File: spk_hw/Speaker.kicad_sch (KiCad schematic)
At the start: 16 parts, among them SW1 SW_SPST, U1 CH591F, U2 MAX98357A, U4 ME6206A33XG, Y1 32MHz

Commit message: spk_hw: Add DC-DC (Migration@tangibles)
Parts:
- added L1: 22u, Inductor_SMD:L_Sunlord_SWPA252012S, symbol Device:L
- C1: value 100n -> 2.2u
- C2: value 1u -> 2.2u
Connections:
- net VDCID: now also L1.1; no longer U1.4 (VSW)
- new net: L1.2, U1.4 (VSW)
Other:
- moved on the sheet: C2

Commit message: spk_hw: Finish schematic, finally >-<
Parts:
- removed SW1: SW_SPST, symbol Switch:SW_SPST
- added C2, C41, C7: 100n, Capacitor_SMD:C_0402_1005Metric, symbol Device:C
- added C31, C32, C33: 10u, Capacitor_SMD:C_0402_1005Metric, symbol Device:C
- added C61, C62, C63, C64: 10u, Capacitor_SMD:C_0603_1608Metric, symbol Device:C
- added C90: 1.5F 5.5V, Capacitor_THT:DX_5R5VxxxxU_D19.0mm_P5.00mm, symbol Device:C_Polarized
- added D2: 1N5819, Diode_SMD:D_SOD-323, symbol Device:D
- added J1: Conn_01x04, TestPoints_P2.00:TestPoints_1x04_P2.00, symbol Connector_Generic:Conn_01x04
- added L2: 2.2u, Inductor_SMD:L_Sunlord_SWPA252012S, symbol Device:L
- added L3: 22u, Inductor_SMD:L_Sunlord_SWPA252012S, symbol Device:L
- added R2, R31: 750k, Resistor_SMD:R_0402_1005Metric, symbol Device:R
- added R3: 100k, Resistor_SMD:R_0402_1005Metric, symbol Device:R
- added R32: 200k, Resistor_SMD:R_0402_1005Metric, symbol Device:R
- added R41, R42: 1M, Resistor_SMD:R_0402_1005Metric, symbol Device:R
- added SC1: Solar_Cell, Connector_JST:JST_PH_S2B-PH-SM4-TB_1x02-1MP_P2.00mm_Horizontal, symbol Device:Solar_Cell
- added SW1: SW_Push, Button_Switch_SMD:SW_SPST_SKQG_WithStem, symbol Switch:SW_Push
- added U3: TPS61099DRV, Package_SON:WSON-6-1EP_2x2mm_P0.65mm_EP1x1.6mm, symbol Regulator_Switching:TPS61099DRV
- added U4: XS3A1T3157, XS3A1T3157:XS3A1T3157GSH, symbol XS3A1T3157:XS3A1T3157
- added U6: MT3608L, Package_TO_SOT_SMD:SOT-23-6, symbol Regulator_Switching:MT3608
- C4: renamed from C3; value 1u -> 2.2u
- C6: renamed from C5; value 100n -> 10u; footprint Capacitor_SMD:C_0402_1005Metric -> Capacitor_SMD:C_0603_1608Metric
- L1: Mfr PN (none) -> SWPA252012S220MT
- LS1: footprint (none) -> Connector_JST:JST_PH_S2B-PH-SM4-TB_1x02-1MP_P2.00mm_Horizontal
- U5: renamed from U4; value ME6206A33XG -> XC6206P332; LCSC PN (none) -> C5446
- renumbered C2 to C3, C4 to C5, C7 to C51, C8 to C52
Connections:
- net BOOT_ACT: now also R1.1; no longer D1.1 (K)
- net GND: now also D1.1 (K), LS1.MP, C2.2, C31.1, C32.1, C33.1, C41.1, C61.1, C62.1, C63.1, C64.1, C7.1, C90.2, J1.2 (Pin_2), R3.2, R32.2, R41.2, R42.1, SC1.2 (-), SC1.MP, U3.1 (GND), U3.7 (GND), U4.2 (GND), U6.2 (GND)
- net VBAT: now also C32.2, C33.2, C41.2, C90.1, R31.1, SW1.1, U3.2 (VOUT), U4.1 (Y2), U4.5 (VCC); no longer C51.2, U5.3 (VI)
- net PWR_LATCH: now reaches U1.10 (PB13/SCK0_/TXD1_/DCD_)
- net PWR_LATCH: now also R41.1, U4.6 (S)
- net RXD: now reaches U1.6 (PA8/RXD1)
- net RXD: now also J1.3 (Pin_3)
- net TXD: now reaches U1.7 (PA9/TMR0/TXD1)
- net TXD: now also J1.4 (Pin_4)
- net BTN: now reaches U1.9 (PB14/TIO/MOSI_/PWM10/DSR)
- net BTN: now also R42.2, SW1.2, U4.3 (Y1)
- net VDD renamed +3.3V
- net +3.3V: now also C2.1, J1.1 (Pin_1); no longer C6.2, R1.1, U2.A1 (~{SD_MODE}), U2.A2 (VDD)
- new net: C31.2, L2.1, SC1.1 (+), U3.4 (EN), U3.6 (VI)
- new net: R31.2, R32.1, U3.3 (FB)
- new net: L2.2, U3.5 (SW)
- new net: D2.2 (A), L3.2, U6.1 (SW)
- new net: R2.2, R3.1, U6.3 (FB)
- new net +5V: C6.2, C63.2, C64.2, C7.2, D2.1 (K), R2.1, U2.A1 (~{SD_MODE}), U2.A2 (VDD)
- new net VBAT_SW: C51.2, C61.2, C62.2, L3.1, U4.4 (Z), U5.3 (VI), U6.4 (EN), U6.5 (IN)
- no-connect marks 17 -> 13
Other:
- note added: "0.6 V typ."
- note added: "1.0 V typ."
- note added: "4.75 V"
- note added: "5.1 V"
- note added: "Shorting the LED pulls BOOT low; LED's Vf is large enough. To be absolutely sure, set BOOT to PB11 in user configuration"
- note added: "min. 50 nA * 100 = 5 uA max. 1 V / 5 uA = 200 kOhm"
- moved on the sheet: AE1, C1, C3, C4, C5, C51, C52, C6, D1, L1, R1, U1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

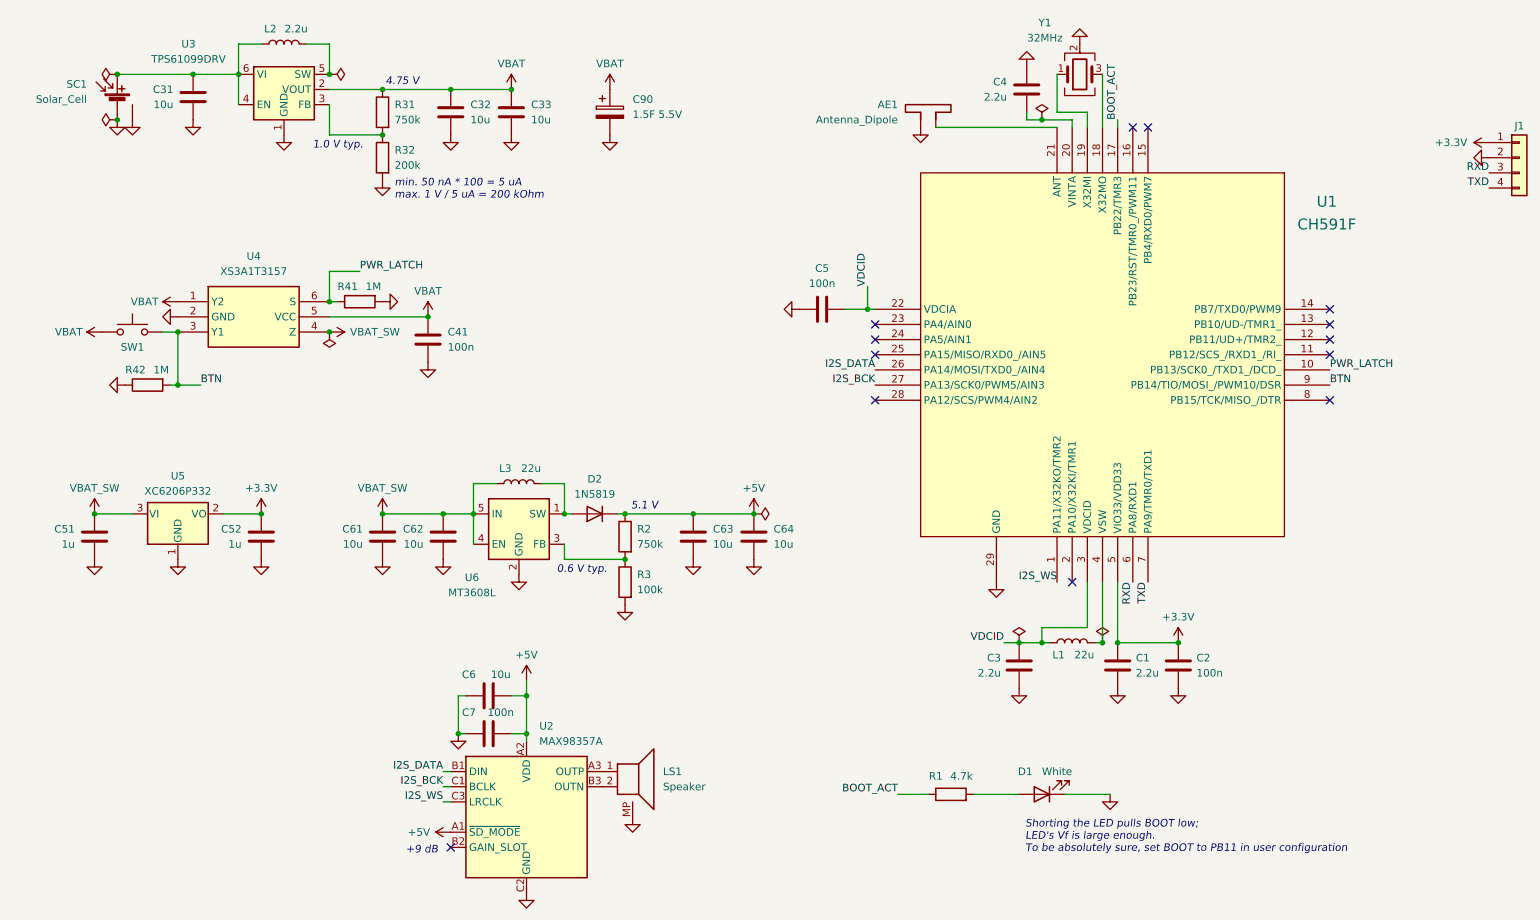
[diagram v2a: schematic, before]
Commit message: spk_hw: Board layout and routing
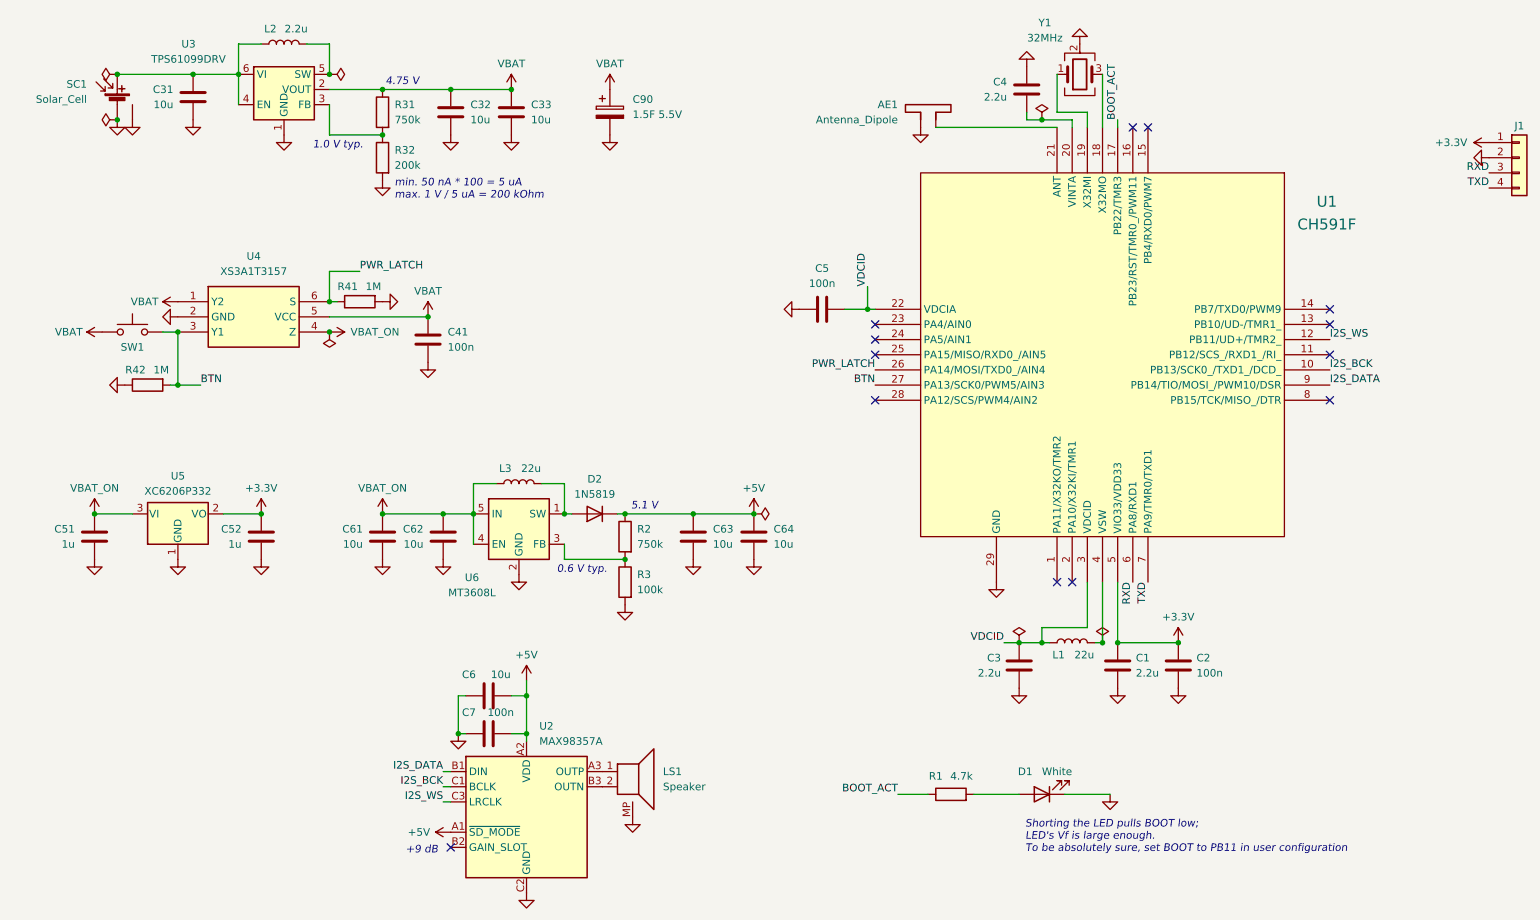
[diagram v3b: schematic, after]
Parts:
- C31, C32, C33: footprint Capacitor_SMD:C_0402_1005Metric -> Capacitor_SMD:C_0603_1608Metric
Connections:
- net BTN: now also U1.27 (PA13/SCK0/PWM5/AIN3); no longer U1.9 (PB14/TIO/MOSI_/PWM10/DSR)
- net I2S_BCK: now also U1.10 (PB13/SCK0_/TXD1_/DCD_); no longer U1.27 (PA13/SCK0/PWM5/AIN3)
- net I2S_DATA: now also U1.9 (PB14/TIO/MOSI_/PWM10/DSR); no longer U1.26 (PA14/MOSI/TXD0_/AIN4)
- net I2S_WS: now also U1.12 (PB11/UD+/TMR2_); no longer U1.1 (PA11/X32KO/TMR2)
- net PWR_LATCH: now also U1.26 (PA14/MOSI/TXD0_/AIN4); no longer U1.10 (PB13/SCK0_/TXD1_/DCD_)
- net VBAT_SW renamed VBAT_ON
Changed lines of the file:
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@@
 	)
 	(no_connect
+		(at 189.23 114.3)
+	)
+	(no_connect
 		(at 158.75 76.2)
 	)
@@
 	)
 	(no_connect
-		(at 234.95 73.66)
-	)
-	(no_connect
 		(at 234.95 68.58)
 	)
@@
 	)
 	(label "I2S_BCK"
-		(at 158.75 81.28 180)
+		(at 234.95 78.74 0)
 		(effects
 			(font
 				(size 1.27 1.27)
 			)
-			(justify right bottom)
+			(justify left bottom)
 		)
 	)
@@
 	)
 	(label "PWR_LATCH"
-		(at 234.95 78.74 0)
+		(at 158.75 78.74 180)
 		(effects
 			(font
 				(size 1.27 1.27)
 			)
-			(justify left bottom)
+			(justify right bottom)
 		)
 	)
@@
 	)
 	(label "I2S_WS"
-		(at 189.23 114.3 180)
+		(at 234.95 73.66 0)
 		(effects
 			(font
 				(size 1.27 1.27)
 			)
-			(justify right bottom)
+			(justify left bottom)
 		)
 	)
@@
 	)
 	(label "BTN"
-		(at 234.95 81.28 0)
+		(at 158.75 81.28 180)
 		(effects
 			(font
 				(size 1.27 1.27)
 			)
-			(justify left bottom)
+			(justify right bottom)
 		)
 	)
@@
 	)
 	(label "I2S_DATA"
-		(at 158.75 78.74 180)
+		(at 234.95 81.28 0)
 		(effects
 			(font
 				(size 1.27 1.27)
 			)
-			(justify right bottom)
+			(justify left bottom)
 		)
 	)
@@
 			)
 		)
-		(property "Footprint" "Capacitor_SMD:C_0402_1005Metric"
+		(property "Footprint" "Capacitor_SMD:C_0603_1608Metric"
 			(at 98.7552 31.75 0)
 			(effects
@@
 			)
 		)
-		(property "Value" "VBAT_SW"
+		(property "Value" "VBAT_ON"
 			(at 76.2 98.552 0)
 			(effects
@@
 			)
 		)
-		(property "Value" "VBAT_SW"
+		(property "Value" "VBAT_ON"
 			(at 27.94 98.552 0)
 			(effects
@@
 			)
 		)
-		(property "Footprint" "Capacitor_SMD:C_0402_1005Metric"
+		(property "Footprint" "Capacitor_SMD:C_0603_1608Metric"
 			(at 43.4848 29.21 0)
 			(effects
@@
 			)
 		)
-		(property "Value" "VBAT_SW"
+		(property "Value" "VBAT_ON"
 			(at 74.93 72.39 90)
 			(effects
@@
 			)
 		)
-		(property "Footprint" "Capacitor_SMD:C_0402_1005Metric"
+		(property "Footprint" "Capacitor_SMD:C_0603_1608Metric"
 			(at 88.5952 31.75 0)
 			(effects

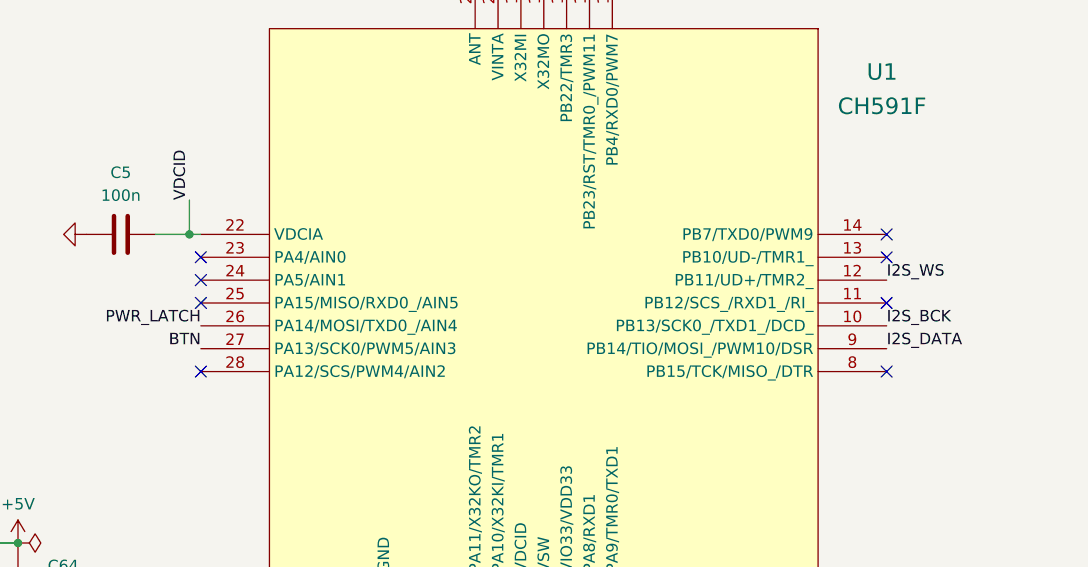
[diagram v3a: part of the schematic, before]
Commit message: spk_hw: Add many vias
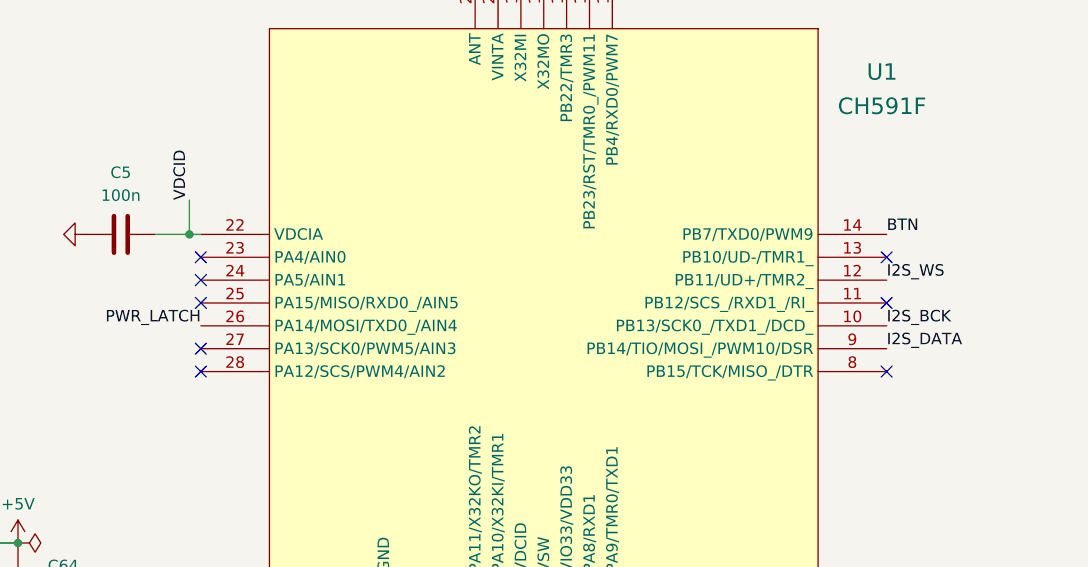
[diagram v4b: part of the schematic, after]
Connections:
- net BTN: now also U1.14 (PB7/TXD0/PWM9); no longer U1.27 (PA13/SCK0/PWM5/AIN3)
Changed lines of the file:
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@@
 	)
 	(no_connect
-		(at 234.95 68.58)
+		(at 158.75 81.28)
 	)
 	(wire
@@
 	)
 	(label "BTN"
-		(at 158.75 81.28 180)
-		(effects
-			(font
-				(size 1.27 1.27)
-			)
-			(justify right bottom)
-		)
-	)
+		(at 234.95 68.58 0)
+		(effects
+			(font
+				(size 1.27 1.27)
+			)
+			(justify left bottom)
+		)
+	)

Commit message: spk_hw: Increase BGA pad size due to fabricator constraints >_<
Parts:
- SW1: LCSC PN (none) -> C318884
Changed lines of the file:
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@@
+			)
+		)
+		(property "LCSC PN" "C318884"
+			(at 34.29 72.39 0)
+			(effects
+				(font
+					(size 1.27 1.27)
+				)
+				(hide yes)
 			)
 		)
